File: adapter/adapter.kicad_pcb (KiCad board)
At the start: 2 copper layers, 43.5 x 38.6 mm, 23 parts, among them J2 Conn_01x06_Female, SW1 RotaryEncoder_Switch

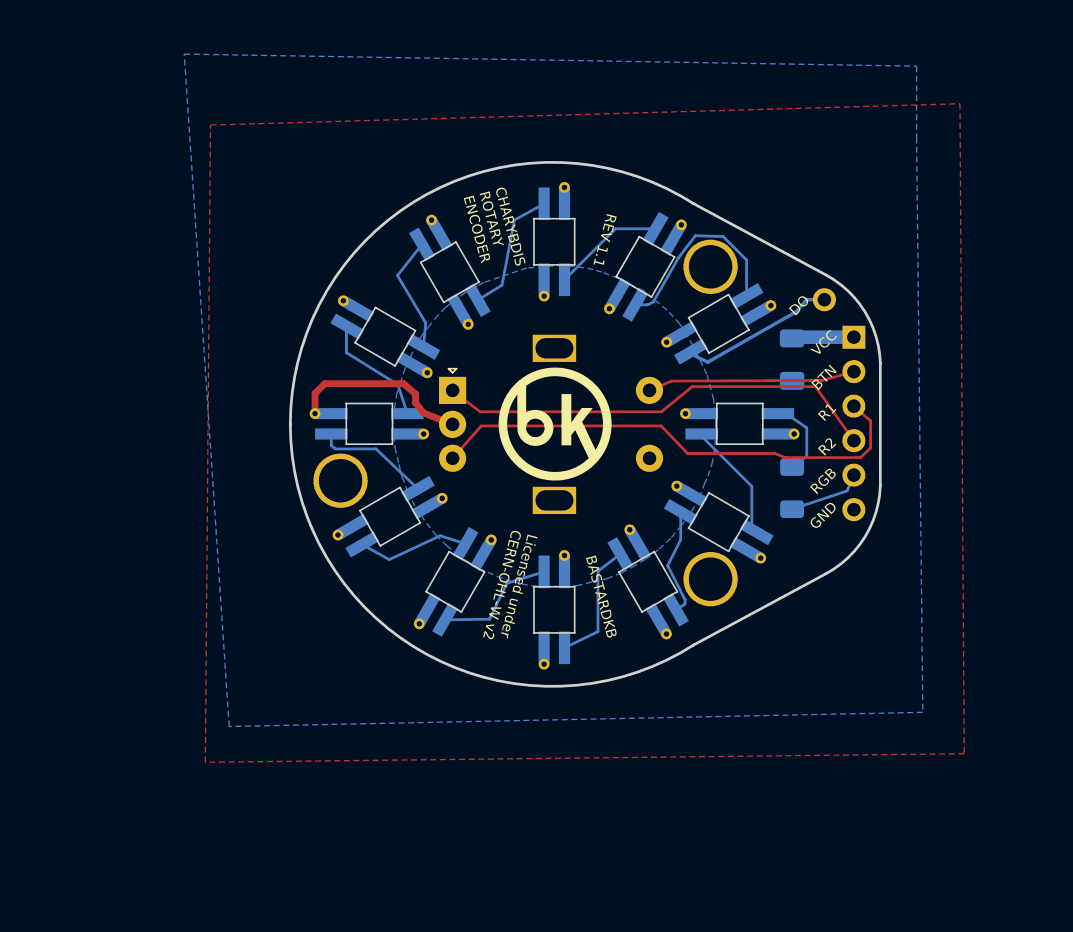
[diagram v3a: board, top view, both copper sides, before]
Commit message: added row/col pin headers and jumpers for sw1 sw2
Bodging the ec11 sw1 and sw2 pins to a free spot in the thumb cluster matrix would allow the pushbutton function to be mapped without needing a custom matrix.c code. Diode footprint added to support this.
Jumpers added to allow selection between direct pin and matrix implementation
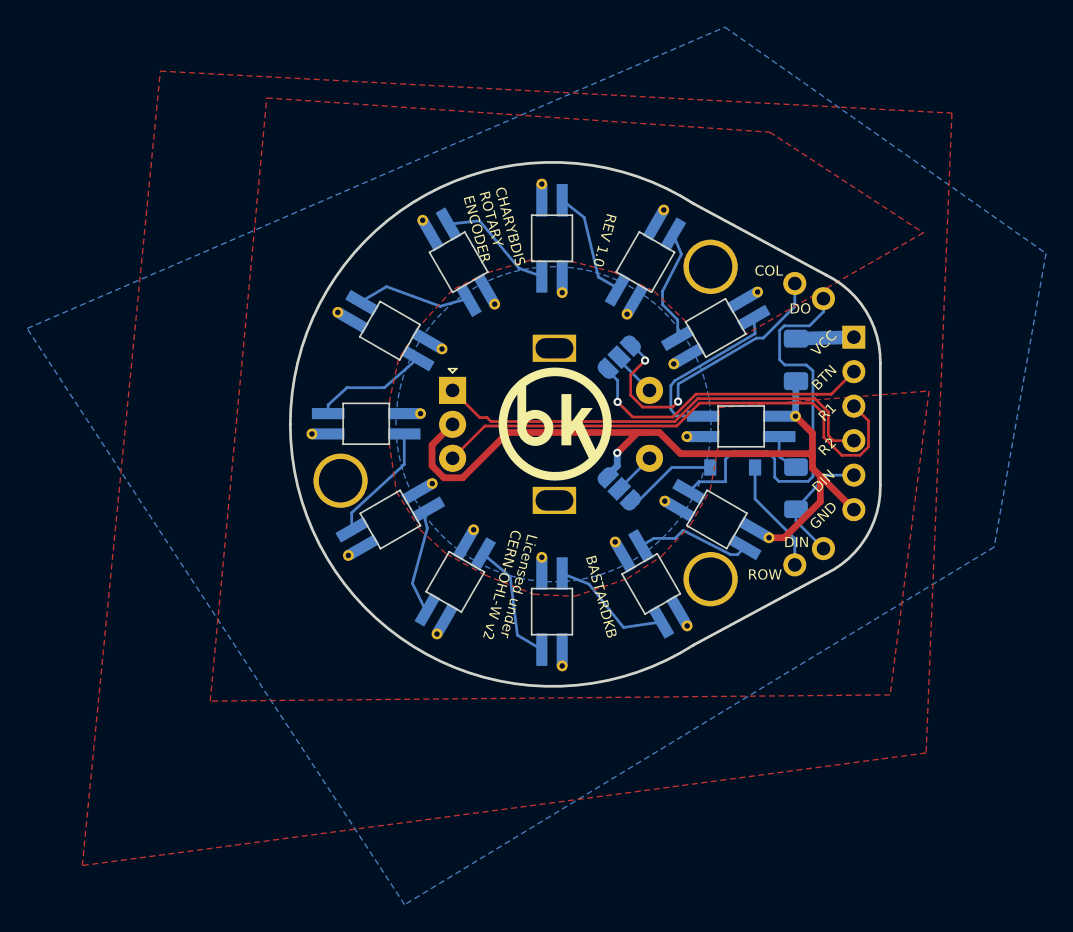
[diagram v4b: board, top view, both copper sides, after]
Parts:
- removed the ? at (72.4, 34.4)
- removed REF** (x12): diy SK6812MINI-E, Library:diy SK6812MINI-E
- added D1: SK6812MINI, Library:YS-SK6812MINI-E, B.Cu at (66.2, 43.8)
- added D10: SK6812MINI, Library:YS-SK6812MINI-E, B.Cu at (38.6, 43.6)
- added D11: SK6812MINI, Library:YS-SK6812MINI-E, B.Cu at (64.5, 50.6)
- added D12: SK6812MINI, Library:YS-SK6812MINI-E, B.Cu at (40.4, 50.6)
- added D2: SK6812MINI, Library:YS-SK6812MINI-E, B.Cu at (52.3, 29.9)
- added D3: SK6812MINI, Library:YS-SK6812MINI-E, B.Cu at (64.4, 36.5)
- added D4: SK6812MINI, Library:YS-SK6812MINI-E, B.Cu at (45.4, 31.7)
- added D5: SK6812MINI, Library:YS-SK6812MINI-E, B.Cu at (59.2, 31.6)
- added D6: SK6812MINI, Library:YS-SK6812MINI-E, B.Cu at (40.4, 36.7)
- added D7: SK6812MINI, Library:YS-SK6812MINI-E, B.Cu at (45.2, 55.2)
- added D8: SK6812MINI, Library:YS-SK6812MINI-E, B.Cu at (52.3, 57.4)
- added D9: SK6812MINI, Library:YS-SK6812MINI-E, B.Cu at (59.6, 55.4)
- added Dcol1: 1N4148W, Library:D_SOD-123, B.Cu at (65.6, 46.8)
- added J1: Conn_01x01_Female, Library:1_PinHeader, F.Cu at (72.3, 34.3)
- added J3: Conn_01x01_Female, Library:1_PinHeader, F.Cu at (72.3, 52.8)
- added J4: Conn_01x01_Female, Library:1_PinHeader, F.Cu at (70.2, 54.0)
- added J5: Conn_01x01_Female, Library:1_PinHeader, F.Cu at (70.2, 33.2)
- added JP1: SolderJumper_3_Open, Library:SolderJumper-3_P1.3mm_Open_RoundedPad1.0x1.5mm, B.Cu at (57.3, 48.4)
- added JP2: SolderJumper_3_Open, Library:SolderJumper-3_P1.3mm_Open_RoundedPad1.0x1.5mm reversed, B.Cu at (57.3, 38.6)
- moved C1 0.29 mm to (70.3, 38.9)
- moved R1 0.29 mm to (70.3, 48.3), turned to -90 degrees
- renumbered C to C1, R to R1
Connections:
- R1 pad 1: DIN -> Net-(D1-Pad3)
- SW1 pad S1: Vcc -> Net-(JP1-Pad2)
- SW1 pad S2: button -> Net-(JP2-Pad2)
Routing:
- net Gnd: track 13.4 -> 59.0 mm, vias 0 -> 1
- net DOUT: track 0.00 -> 30.6 mm
- net Row: track 0.00 -> 22.1 mm, vias 0 -> 2
- net Net-(D11-D12): track 14.3 -> 0.00 mm
- net Net-(D1-Pad1): track 0.00 -> 12.8 mm
- net DO: track 11.5 -> 0.00 mm
- net Net-(D9-D10): track 9.48 -> 0.00 mm
- net Net-(D3-D4): track 9.26 -> 0.00 mm
- net Net-(D4-D5): track 9.08 -> 0.00 mm
- net Net-(D7-Pad1): track 0.00 -> 9.03 mm
- net Net-(D8-Pad1): track 0.00 -> 9.02 mm
- net Net-(D1-D2): track 8.99 -> 0.00 mm
- net Net-(D8-D9): track 8.76 -> 0.00 mm
- net Net-(D7-D8): track 8.70 -> 0.00 mm
- net Net-(D11-Pad3): track 0.00 -> 8.69 mm
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- added copper zone on F.Cu, net Gnd
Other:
- board text added: "COL"
- board text added: "DIN"
- board text added: "REV 1.0"
- board text added: "ROW"
- board text removed: "REV 1.1"
- board text removed: "RGB"

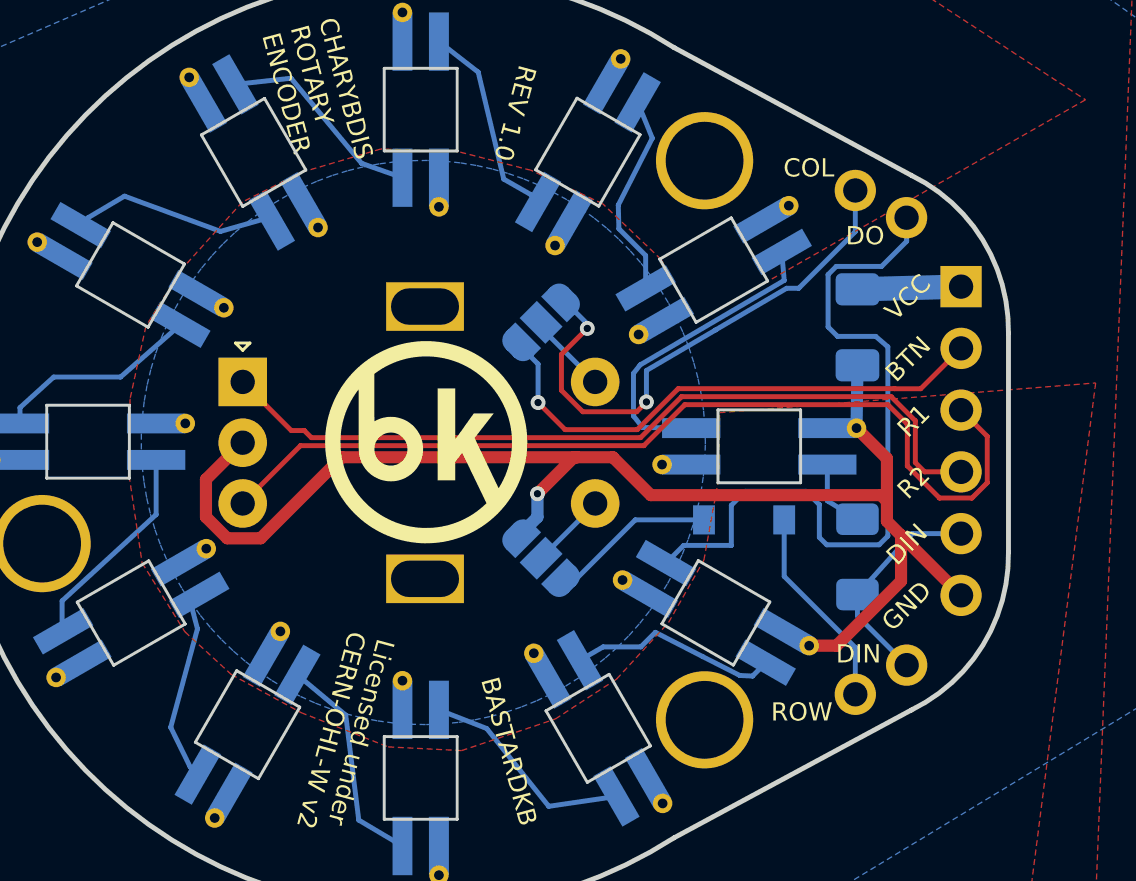
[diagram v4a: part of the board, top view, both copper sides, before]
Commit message: rearranged pins and reroute
reverted BK logo to silkscreen
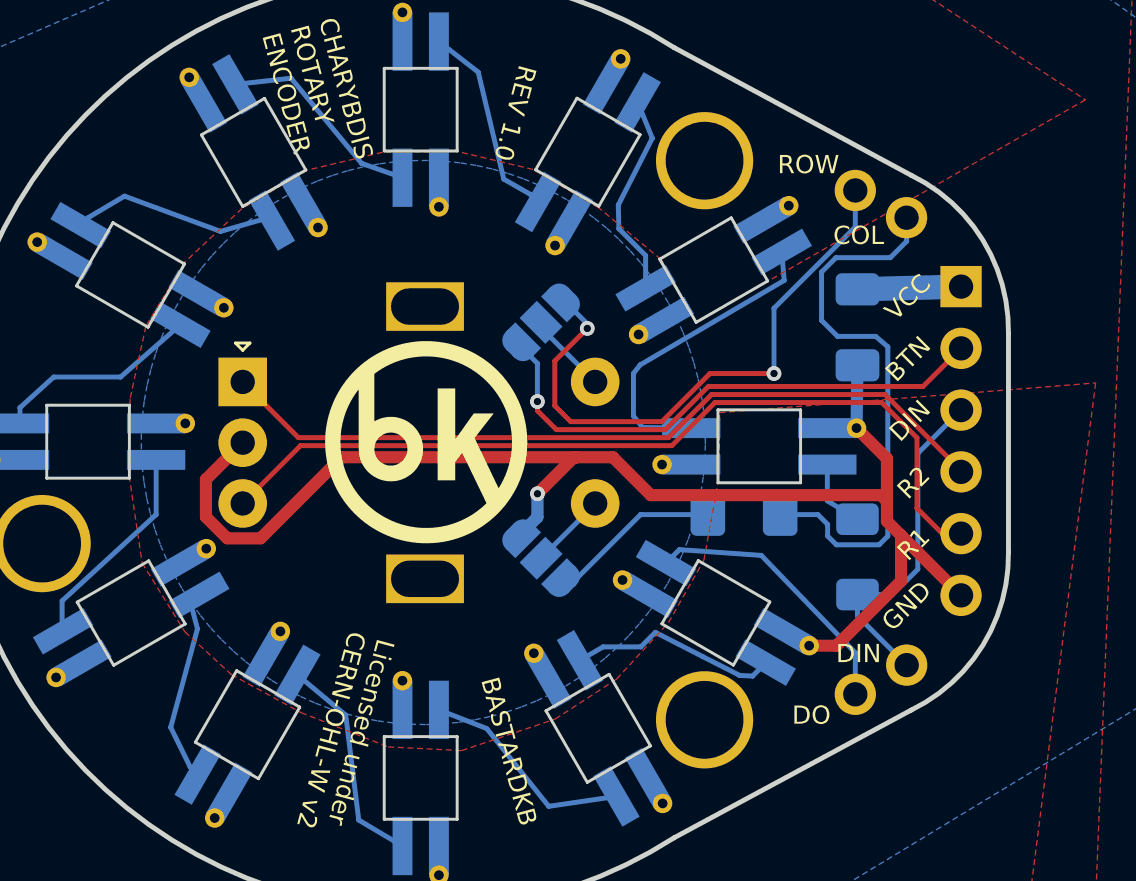
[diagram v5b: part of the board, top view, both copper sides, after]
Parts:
- Dcol1: footprint Library:D_SOD-123 -> Library:D_1206_3216Metric_Pad1.42x1.75mm_HandSolder
- moved Dcol1 0.22 mm to (65.6, 46.6)
- renumbered J2 to J1, J1 to J2, J5 to J3, J3 to J4, J4 to J5
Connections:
- J1 pad 3: r1 -> DIN
- J1 pad 5: DIN -> r1
- J2 pad 1: DOUT -> Col
- J5 pad 1: Col -> DOUT
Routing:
- net DOUT: track 30.6 -> 11.4 mm
- net Col: track 8.39 -> 23.3 mm
- net DIN: track 9.12 -> 13.9 mm
- net r1: track 38.6 -> 35.2 mm
- net Row: track 22.1 -> 24.3 mm
- net r2: track 33.5 -> 32.6 mm

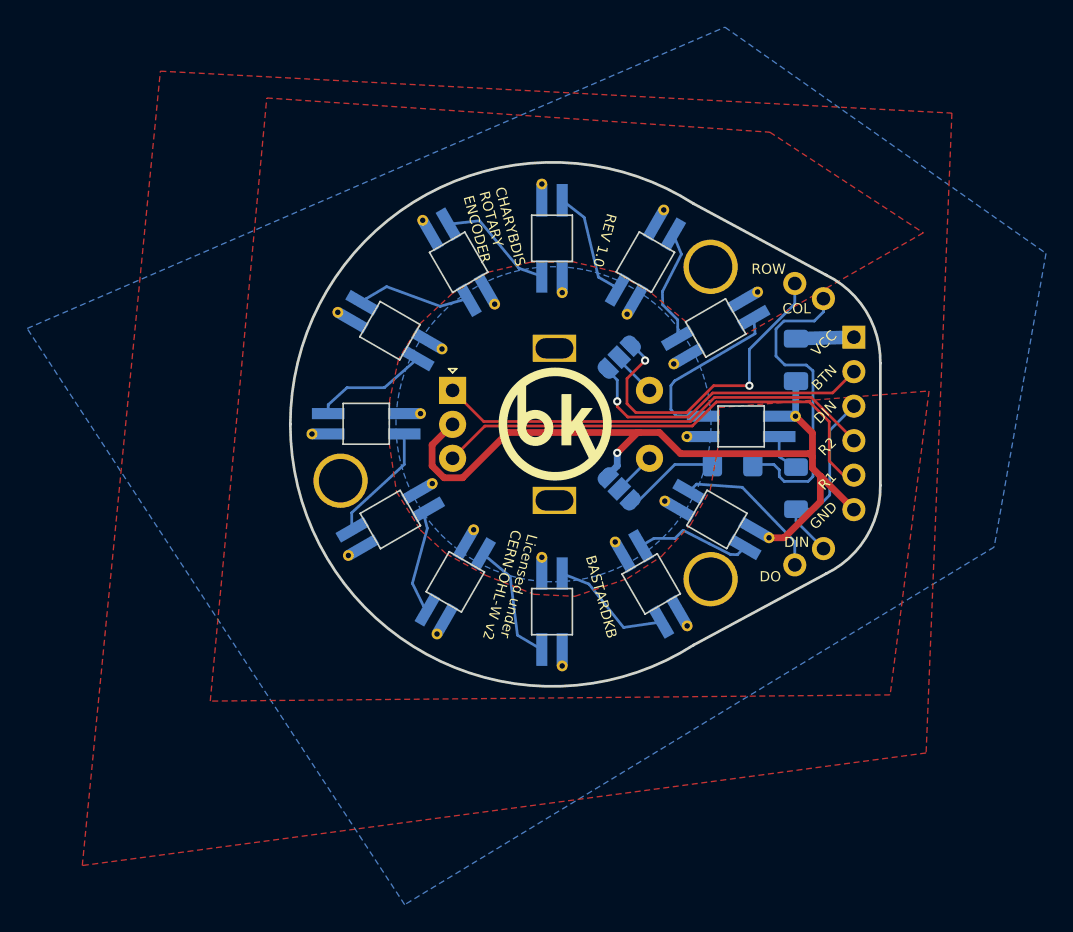
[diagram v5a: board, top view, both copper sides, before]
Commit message: flip LEDs to correct orientation
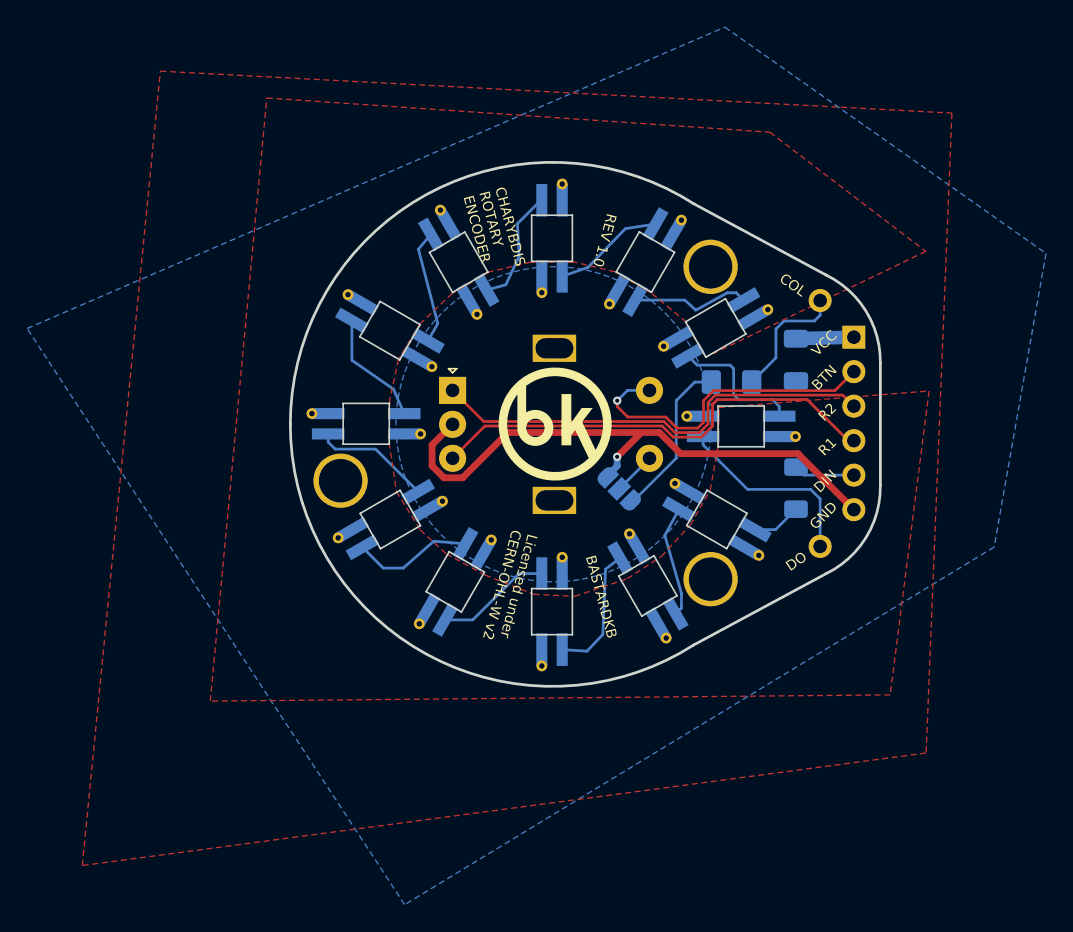
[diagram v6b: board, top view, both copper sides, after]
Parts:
- removed J3, J4: Conn_01x01_Female, Library:1_PinHeader
- removed JP2: SolderJumper_3_Open, Library:SolderJumper-3_P1.3mm_Open_RoundedPad1.0x1.5mm reversed
- moved Dcol1 6.07 mm to (65.5, 40.5)
- moved J5 2.31 mm to (72.1, 52.6)
- moved D2 0.29 mm to (59.4, 55.5), turned to 120 degrees
- moved J2 0.28 mm to (72.1, 34.5)
- turned D1 to 150 degrees
- turned D10 to -120 degrees
- turned D11 to -150 degrees
- turned D12 to 180 degrees
- turned D3 to 90 degrees
- turned D4 to 60 degrees
- turned D5 to 30 degrees
- turned D6 to 0 degrees
- turned D7 to -30 degrees
- turned D8 to -60 degrees
- turned D9 to -90 degrees
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- renumbered D11 to D1, D5 to D10, D3 to D11, D1 to D12, D9 to D2, D8 to D3, D7 to D4, D12 to D5, D10 to D6, D6 to D7, D4 to D8, D2 to D9
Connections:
- D1 pad 1: DOUT -> Net-(D1-Pad1)
- D1 pad 3: Net-(D11-Pad3) -> Net-(D1-Pad3)
- D10 pad 1: Net-(D2-Pad3) -> Net-(D10-Pad1)
- D10 pad 3: Net-(D3-Pad1) -> Net-(D10-Pad3)
- D11 pad 1: Net-(D3-Pad1) -> Net-(D11-Pad1)
- D11 pad 3: Net-(D1-Pad1) -> Net-(D10-Pad1)
- D12 pad 1: Net-(D1-Pad1) -> DOUT
- D12 pad 3: Net-(D1-Pad3) -> Net-(D11-Pad1)
- D2 pad 1: Net-(D11-Pad3) -> Net-(D2-Pad1)
- D2 pad 3: Net-(D8-Pad1) -> Net-(D1-Pad1)
- D3 pad 1: Net-(D8-Pad1) -> Net-(D3-Pad1)
- D3 pad 3: Net-(D7-Pad1) -> Net-(D2-Pad1)
- D4 pad 1: Net-(D7-Pad1) -> Net-(D4-Pad1)
- D4 pad 3: Net-(D12-Pad1) -> Net-(D3-Pad1)
- D5 pad 1: Net-(D12-Pad1) -> Net-(D5-Pad1)
- D5 pad 3: Net-(D10-Pad1) -> Net-(D4-Pad1)
- D6 pad 1: Net-(D10-Pad1) -> Net-(D6-Pad1)
- D6 pad 3: Net-(D10-Pad3) -> Net-(D5-Pad1)
- D7 pad 1: Net-(D10-Pad3) -> Net-(D7-Pad1)
- D7 pad 3: Net-(D4-Pad1) -> Net-(D6-Pad1)
- D8 pad 1: Net-(D4-Pad1) -> Net-(D8-Pad1)
- D8 pad 3: Net-(D2-Pad1) -> Net-(D7-Pad1)
- D9 pad 1: Net-(D2-Pad1) -> Net-(D10-Pad3)
- D9 pad 3: Net-(D2-Pad3) -> Net-(D8-Pad1)
- J1 pad 3: DIN -> r2
- J1 pad 4: r2 -> r1
- J1 pad 5: r1 -> DIN
- SW1 pad S2: Net-(JP2-Pad2) -> button
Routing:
- net Row: track 24.3 -> 0.00 mm, vias 2 -> 0
- net Gnd: track 59.0 -> 43.1 mm
- net Col: track 23.3 -> 9.40 mm
- net Net-(D11-Pad1): track 0.00 -> 10.1 mm
- net DIN: track 13.9 -> 4.51 mm
- net Net-(D5-Pad1): track 0.00 -> 8.74 mm
- net Net-(D11-Pad3): track 8.69 -> 0.00 mm
- net Net-(D6-Pad1): track 0.00 -> 8.62 mm
- net Net-(D2-Pad3): track 8.28 -> 0.00 mm
- net Net-(D12-Pad1): track 8.11 -> 0.00 mm
- net Net-(Dcol1-Pad2): track 7.06 -> 12.0 mm
- net Net-(D1-Pad1): track 12.8 -> 8.31 mm
- net Net-(JP2-Pad2): track 3.37 -> 0.00 mm
- net DOUT: track 11.4 -> 14.4 mm
- net button: track 22.2 -> 23.9 mm
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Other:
- board text removed: "ROW"

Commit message: silkscreen
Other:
- board text added: "REV 1.1"
- board text removed: "REV 1.0"
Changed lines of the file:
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@@
     (effects (font (size 0.75 0.75) (thickness 0.1)))
   )
-  (gr_text "CHARYBDIS \nROTARY \nENCODER" (at 47.3 26.45 285) (layer "F.SilkS")
+  (gr_text "CHARYBDIS \nROTARY \nENCODER" (at 47.413 25.707 285) (layer "F.SilkS")
     (effects (font (size 0.75 0.75) (thickness 0.1)) (justify left))
   )
@@
     (effects (font (size 0.75 0.75) (thickness 0.1)))
   )
-  (gr_text "REV 1.0" (at 56.2 30.05 255) (layer "F.SilkS")
+  (gr_text "REV 1.1" (at 56.2 30.05 255) (layer "F.SilkS")
     (effects (font (size 0.75 0.75) (thickness 0.1)))
   )

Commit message: Update adapter.kicad_pcb
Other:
- board text added: "REV 1.1.2"
- board text removed: "REV 1.1"
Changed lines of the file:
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@@
     (effects (font (size 0.75 0.75) (thickness 0.1)))
   )
-  (gr_text "REV 1.1" (at 56.2 30.05 255) (layer "F.SilkS")
+  (gr_text "REV 1.1.2" (at 56.2 30.05 255) (layer "F.SilkS")
     (effects (font (size 0.75 0.75) (thickness 0.1)))
   )
